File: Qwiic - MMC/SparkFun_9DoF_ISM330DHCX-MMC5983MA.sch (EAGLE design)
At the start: 33 parts, among them J1 QWIIC_RIGHT_ANGLE, J2 QWIIC_RIGHT_ANGLE, U1 ISM330DHCX, U2 MMC5983MA_QFN16

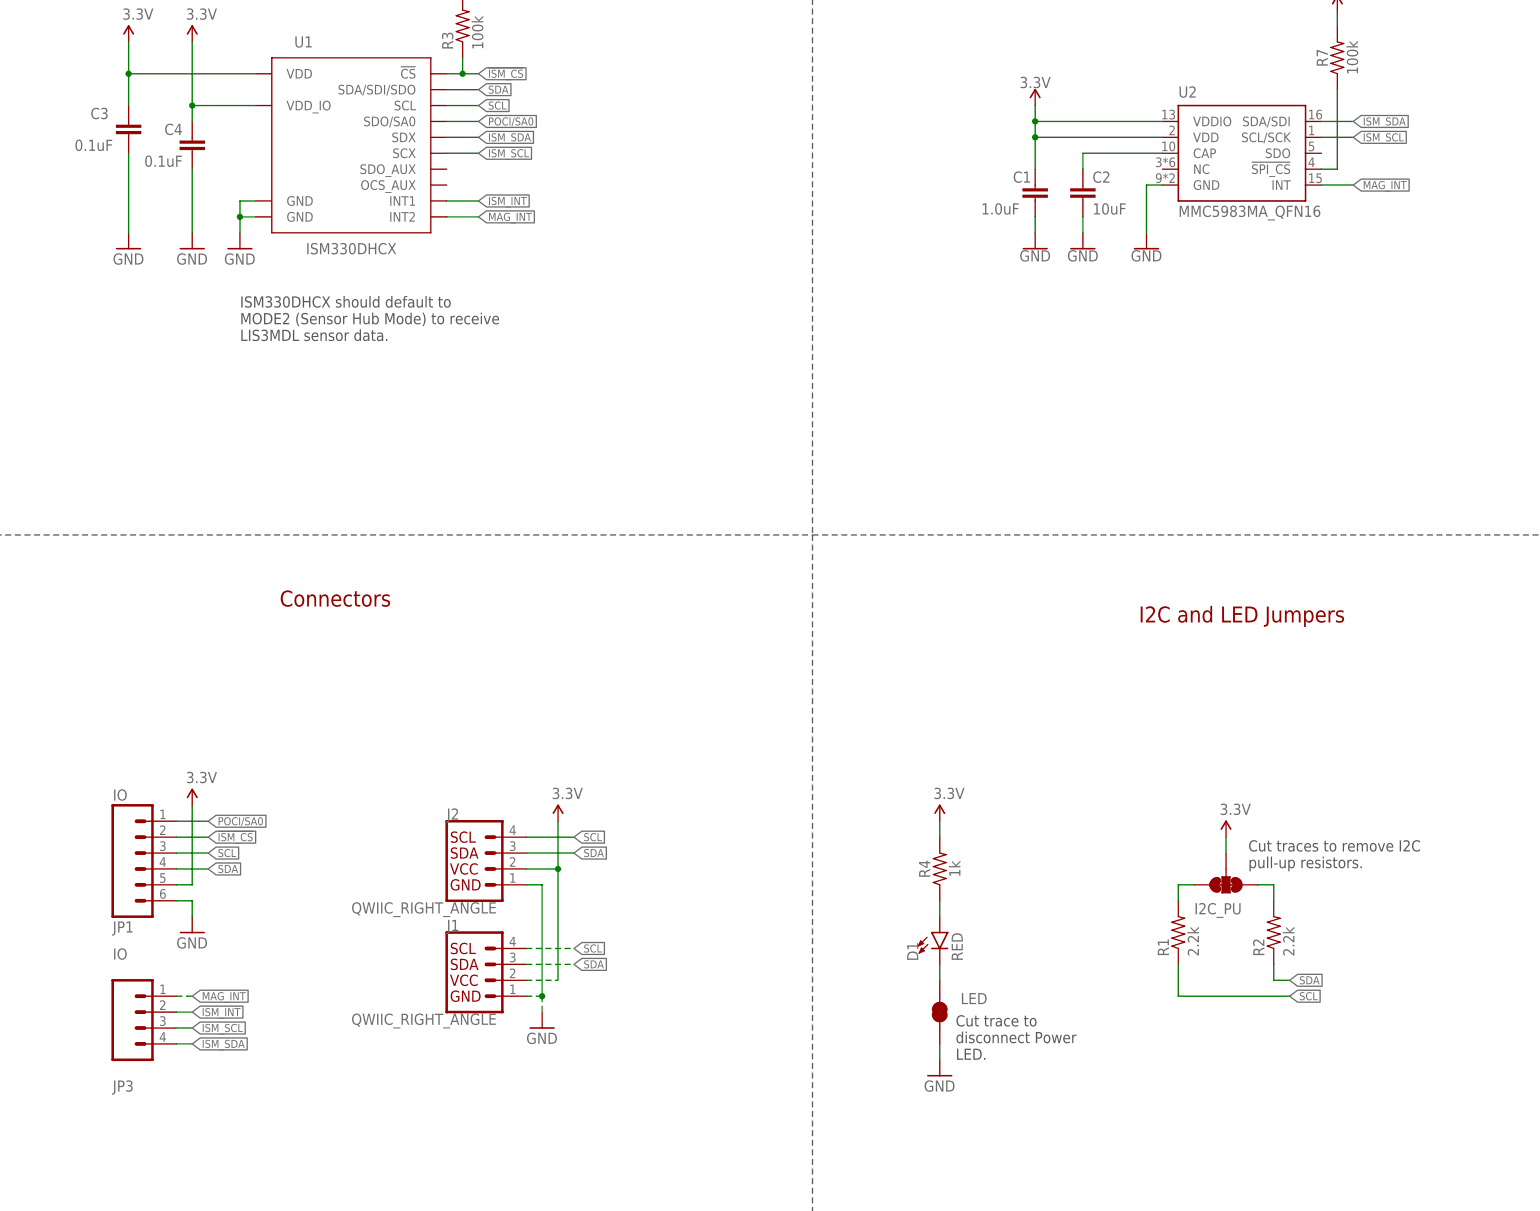
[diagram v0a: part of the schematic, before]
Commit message: Restricts ground pour around Magnetometer, renames 6DoF I2C nets
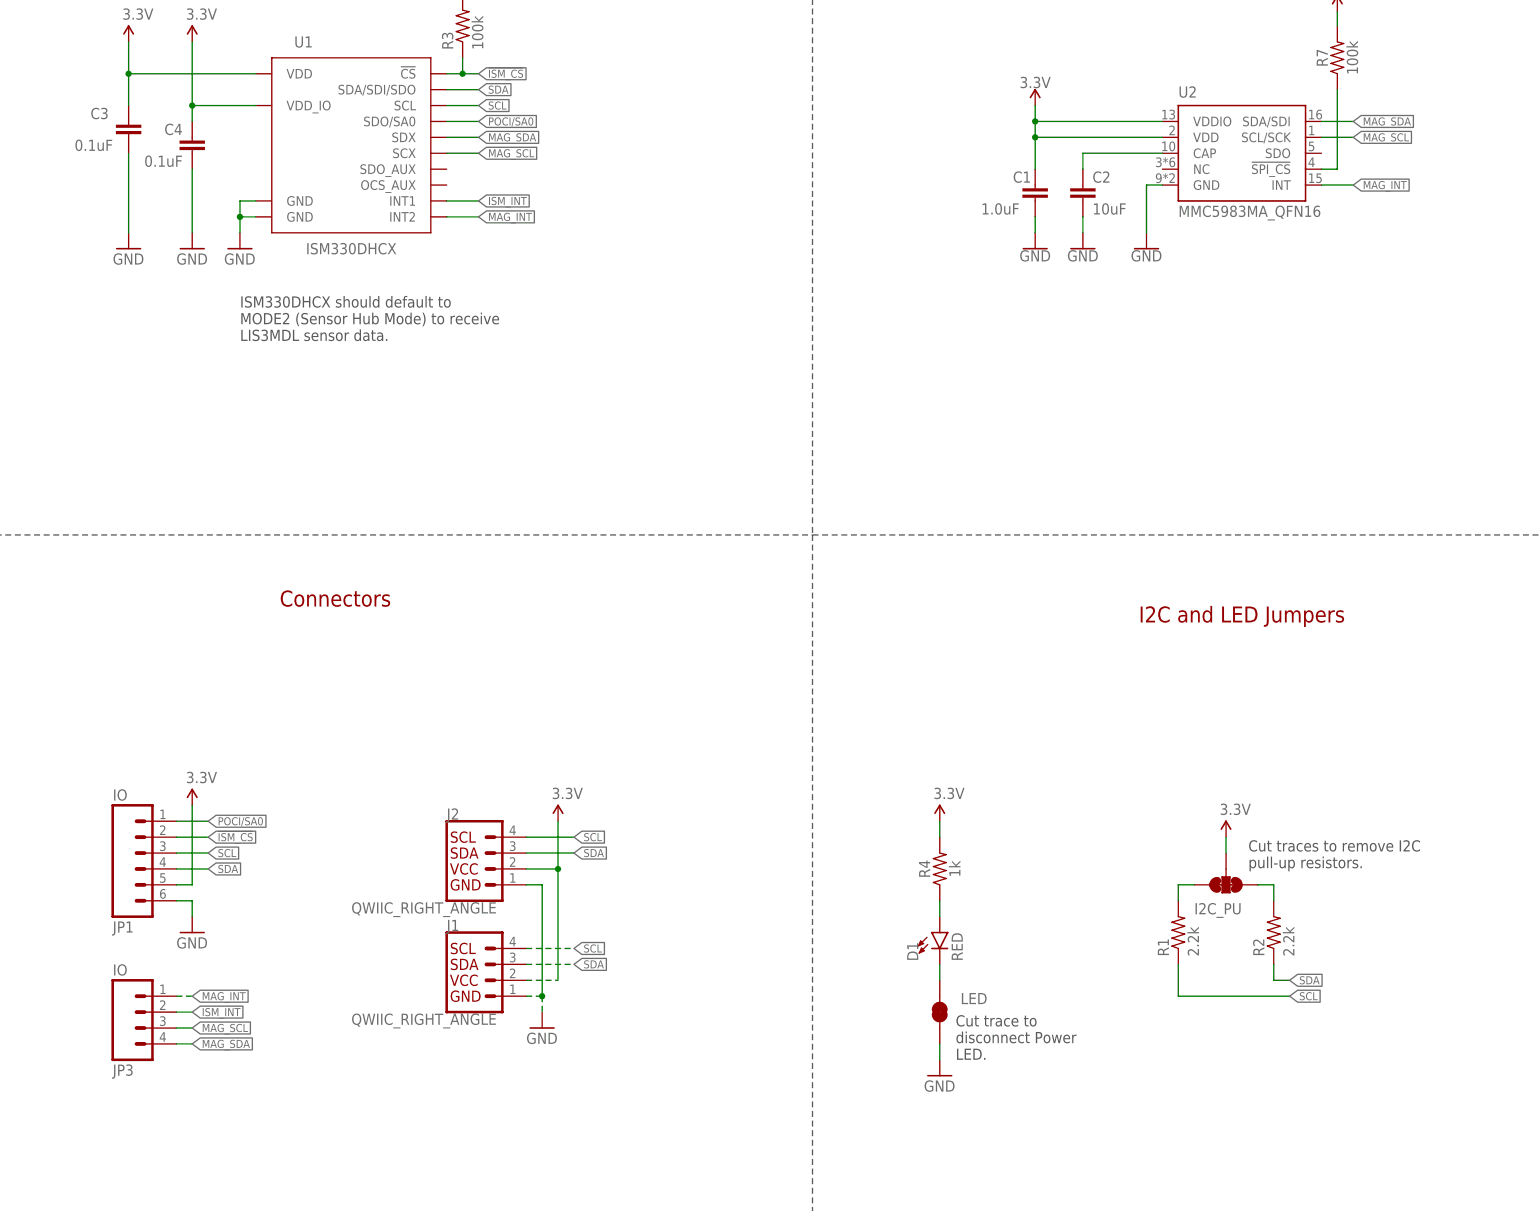
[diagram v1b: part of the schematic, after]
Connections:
- net ISM_SCL renamed MAG_SCL
- net ISM_SDA renamed MAG_SDA
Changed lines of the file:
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@@
 <instance part="LOGO3" gate="G$1" x="373.38" y="33.02" smashed="yes"/>
 <instance part="JP3" gate="J1" x="40.64" y="76.2" smashed="yes" rot="MR180">
-<attribute name="VALUE" x="35.56" y="86.36" size="1.778" layer="96" font="vector" rot="MR180"/>
-<attribute name="NAME" x="35.56" y="65.278" size="1.778" layer="95" font="vector" rot="MR180"/>
+<attribute name="VALUE" x="35.56" y="83.82" size="1.778" layer="96" font="vector" rot="MR180"/>
+<attribute name="NAME" x="35.56" y="67.818" size="1.778" layer="95" font="vector" rot="MR180"/>
 </instance>
 <instance part="J1" gate="G$1" x="93.98" y="81.28" smashed="yes">
@@
 </segment>
 </net>
-<net name="ISM_SCL" class="0">
+<net name="MAG_SCL" class="0">
 <segment>
 <wire x1="88.9" y1="213.36" x2="93.98" y2="213.36" width="0.1524" layer="91"/>
@@
 </segment>
 </net>
-<net name="ISM_SDA" class="0">
+<net name="MAG_SDA" class="0">
 <segment>
 <wire x1="88.9" y1="215.9" x2="93.98" y2="215.9" width="0.1524" layer="91"/>

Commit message: Fixes many silk errors
* Adds polarity marker to MMC - previous one is eaten by PTH silk
* Adds flags to interrupt silk
* Moves resistor to make room for SDA and SCL silk
* Renames "MAG SDA/SCL"  net to "AUX SDA/SCL"
* Rotates version number in copper
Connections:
- net MAG_SCL renamed AUX_SCL
- net MAG_SDA renamed AUX_SDA
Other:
- note added: "(Default)"
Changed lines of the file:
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@@
 <wire x1="370.84" y1="205.74" x2="370.84" y2="198.12" width="0.2032" layer="97"/>
 <wire x1="370.84" y1="198.12" x2="378.46" y2="198.12" width="0.2032" layer="97"/>
-<wire x1="378.46" y1="198.12" x2="393.7" y2="198.12" width="0.2032" layer="97"/>
-<wire x1="393.7" y1="198.12" x2="393.7" y2="205.74" width="0.2032" layer="97"/>
-<wire x1="393.7" y1="205.74" x2="393.7" y2="210.82" width="0.2032" layer="97"/>
-<wire x1="393.7" y1="210.82" x2="393.7" y2="215.9" width="0.2032" layer="97"/>
-<wire x1="393.7" y1="215.9" x2="393.7" y2="220.98" width="0.2032" layer="97"/>
-<wire x1="393.7" y1="220.98" x2="370.84" y2="220.98" width="0.2032" layer="97"/>
+<wire x1="378.46" y1="198.12" x2="403.86" y2="198.12" width="0.2032" layer="97"/>
+<wire x1="403.86" y1="198.12" x2="403.86" y2="205.74" width="0.2032" layer="97"/>
+<wire x1="403.86" y1="205.74" x2="403.86" y2="210.82" width="0.2032" layer="97"/>
+<wire x1="403.86" y1="210.82" x2="403.86" y2="215.9" width="0.2032" layer="97"/>
+<wire x1="403.86" y1="215.9" x2="403.86" y2="220.98" width="0.2032" layer="97"/>
+<wire x1="403.86" y1="220.98" x2="370.84" y2="220.98" width="0.2032" layer="97"/>
 <wire x1="370.84" y1="215.9" x2="378.46" y2="215.9" width="0.2032" layer="97"/>
-<wire x1="378.46" y1="215.9" x2="393.7" y2="215.9" width="0.2032" layer="97"/>
+<wire x1="378.46" y1="215.9" x2="403.86" y2="215.9" width="0.2032" layer="97"/>
 <wire x1="378.46" y1="215.9" x2="378.46" y2="210.82" width="0.2032" layer="97"/>
 <wire x1="378.46" y1="210.82" x2="378.46" y2="205.74" width="0.2032" layer="97"/>
 <wire x1="378.46" y1="205.74" x2="378.46" y2="198.12" width="0.2032" layer="97"/>
-<wire x1="378.46" y1="210.82" x2="393.7" y2="210.82" width="0.2032" layer="97"/>
-<wire x1="378.46" y1="205.74" x2="393.7" y2="205.74" width="0.2032" layer="97"/>
+<wire x1="378.46" y1="210.82" x2="403.86" y2="210.82" width="0.2032" layer="97"/>
+<wire x1="378.46" y1="205.74" x2="403.86" y2="205.74" width="0.2032" layer="97"/>
 <wire x1="378.46" y1="210.82" x2="370.84" y2="210.82" width="0.2032" layer="97"/>
 <wire x1="370.84" y1="205.74" x2="378.46" y2="205.74" width="0.2032" layer="97"/>
@@
 <text x="215.9" y="139.7" size="2.54" layer="94" font="vector" align="center">I2C and LED Jumpers</text>
 <text x="216.916" y="257.048" size="1.27" layer="97" font="vector" align="center">I2C address: 0x30</text>
+<text x="389.636" y="212.598" size="1.778" layer="97" font="vector">(Default)</text>
 </plain>
 <instances>
@@
 </instance>
 <instance part="6DOF_ADDR" gate="G$1" x="358.14" y="223.52" smashed="yes" rot="MR180">
-<attribute name="NAME" x="374.904" y="219.075" size="1.778" layer="95" font="vector" rot="MR180"/>
+<attribute name="NAME" x="379.984" y="219.075" size="1.778" layer="95" font="vector" rot="MR180"/>
 </instance>
 <instance part="GND6" gate="1" x="358.14" y="200.66" smashed="yes" rot="MR0">
@@
 </segment>
 </net>
-<net name="MAG_SCL" class="0">
+<net name="AUX_SCL" class="0">
 <segment>
 <wire x1="88.9" y1="213.36" x2="93.98" y2="213.36" width="0.1524" layer="91"/>
@@
 </segment>
 </net>
-<net name="MAG_SDA" class="0">
+<net name="AUX_SDA" class="0">
 <segment>
 <wire x1="88.9" y1="215.9" x2="93.98" y2="215.9" width="0.1524" layer="91"/>

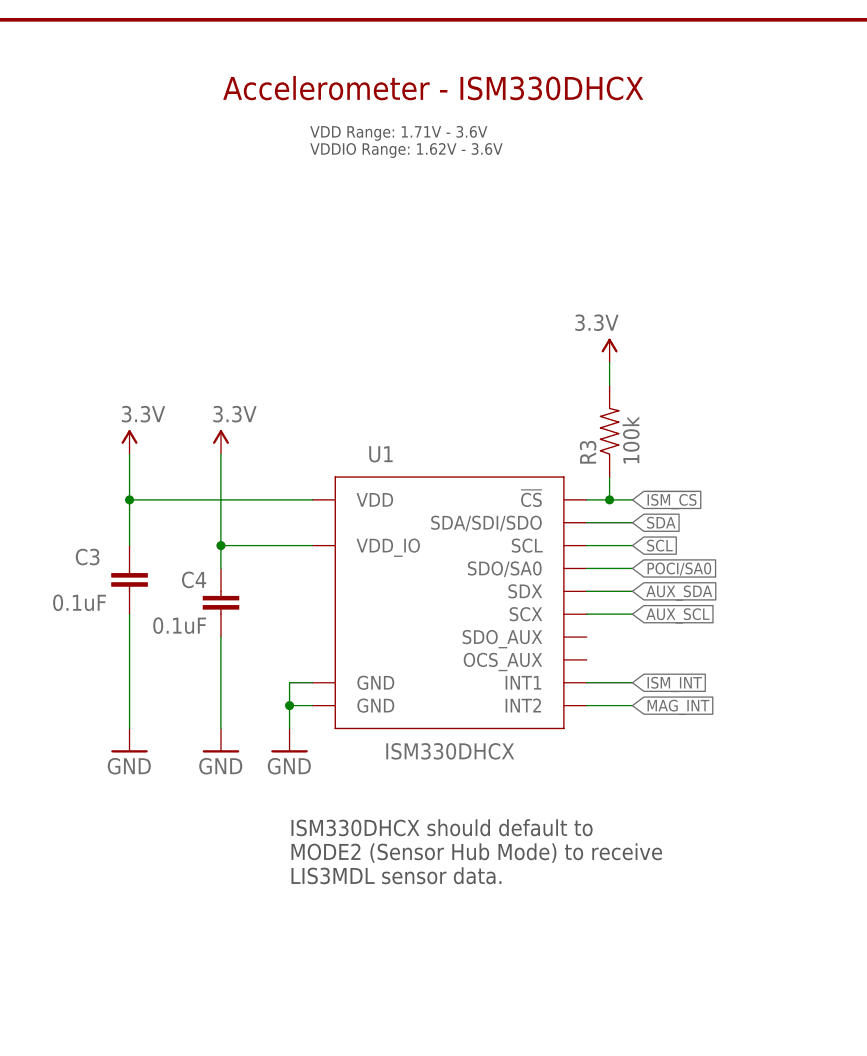
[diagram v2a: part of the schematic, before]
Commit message: Changes main 6DoF to new part
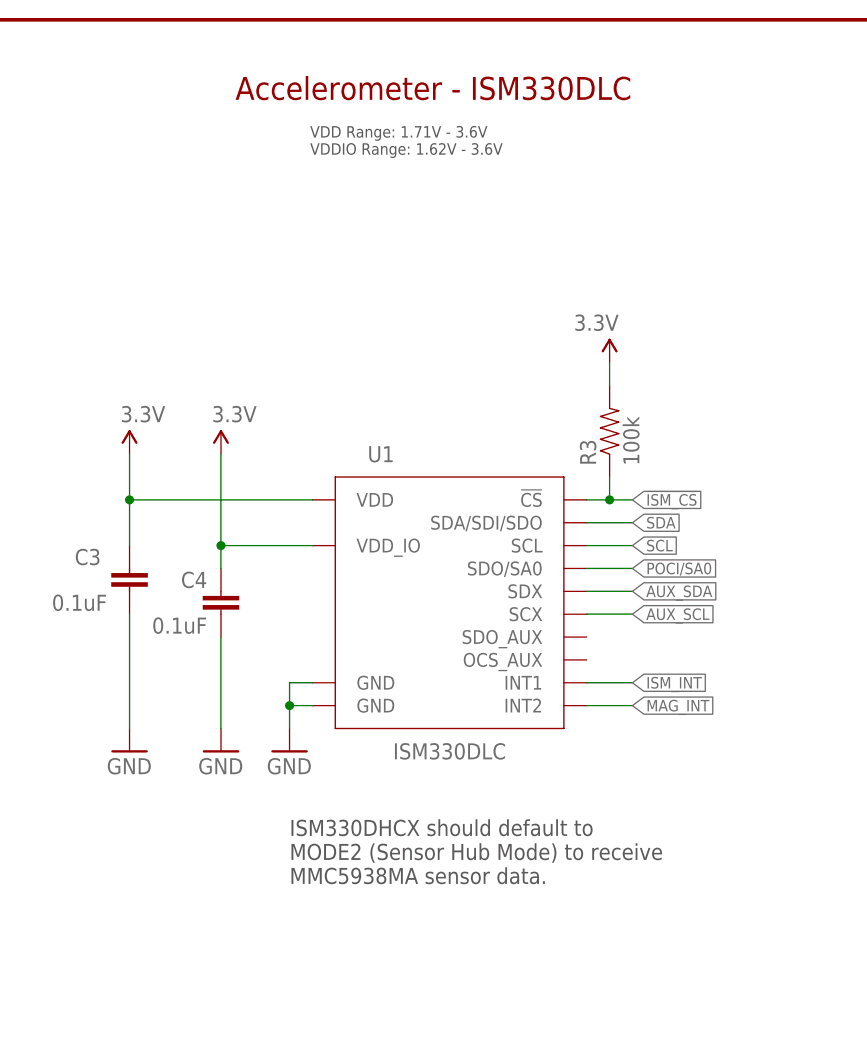
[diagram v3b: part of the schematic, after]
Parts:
- U1: value ISM330DHCX -> ISM330DLC; device ISM330DHCX:ISM330DHCX -> ISM330DLC:ISM330DLC
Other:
- note added: "Accelerometer - ISM330DLC"
- note added: "ISM330DHCX should default to MODE2 (Sensor Hub Mode) to receive MMC5938MA sensor data."
- note removed: "Accelerometer - ISM330DHCX"
- note removed: "ISM330DHCX should default to MODE2 (Sensor Hub Mode) to receive LIS3MDL sensor data."
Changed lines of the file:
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@@
 <part name="R5" library="SparkFun-Resistors" deviceset="100KOHM" device="-0603-1/10W-1%" value="100k"/>
 <part name="SUPPLY5" library="SparkFun-PowerSymbols" deviceset="3.3V" device=""/>
-<part name="U1" library="ISM330DHCX" deviceset="ISM330DHCX" device=""/>
+<part name="U1" library="ISM330DLC" deviceset="ISM330DLC" device=""/>
 <part name="R6" library="SparkFun-Resistors" deviceset="100KOHM" device="-0603-1/10W-1%" value="100k"/>
 <part name="FRAME2" library="SparkFun-Aesthetics" deviceset="FRAME-LEDGER" device=""/>
@@
 <sheet>
 <plain>
-<text x="71.882" y="271.78" size="2.54" layer="94" font="vector" align="center">Accelerometer - ISM330DHCX</text>
+<text x="71.882" y="271.78" size="2.54" layer="94" font="vector" align="center">Accelerometer - ISM330DLC</text>
 <text x="216.916" y="103.632" size="1.778" layer="97" font="vector" align="top-left">Cut traces to remove I2C
 pull-up resistors.</text>
 <text x="55.88" y="190.5" size="1.778" layer="97" font="vector" align="top-left">ISM330DHCX should default to
 MODE2 (Sensor Hub Mode) to receive
-LIS3MDL sensor data.
+MMC5938MA sensor data.
 </text>
 <text x="58.166" y="264.414" size="1.27" layer="97" font="vector">VDD Range: 1.71V - 3.6V
